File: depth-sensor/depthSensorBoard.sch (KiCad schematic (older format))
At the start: 16 parts, among them P1 CONN_02X05, P3 CONN_01X04, P4 CONN_01X04, P5 CONN_01X04, P6 CONN_01X04, Q2 Q_NJFET_GSD, U1 AP2112, U2 TCA9545A

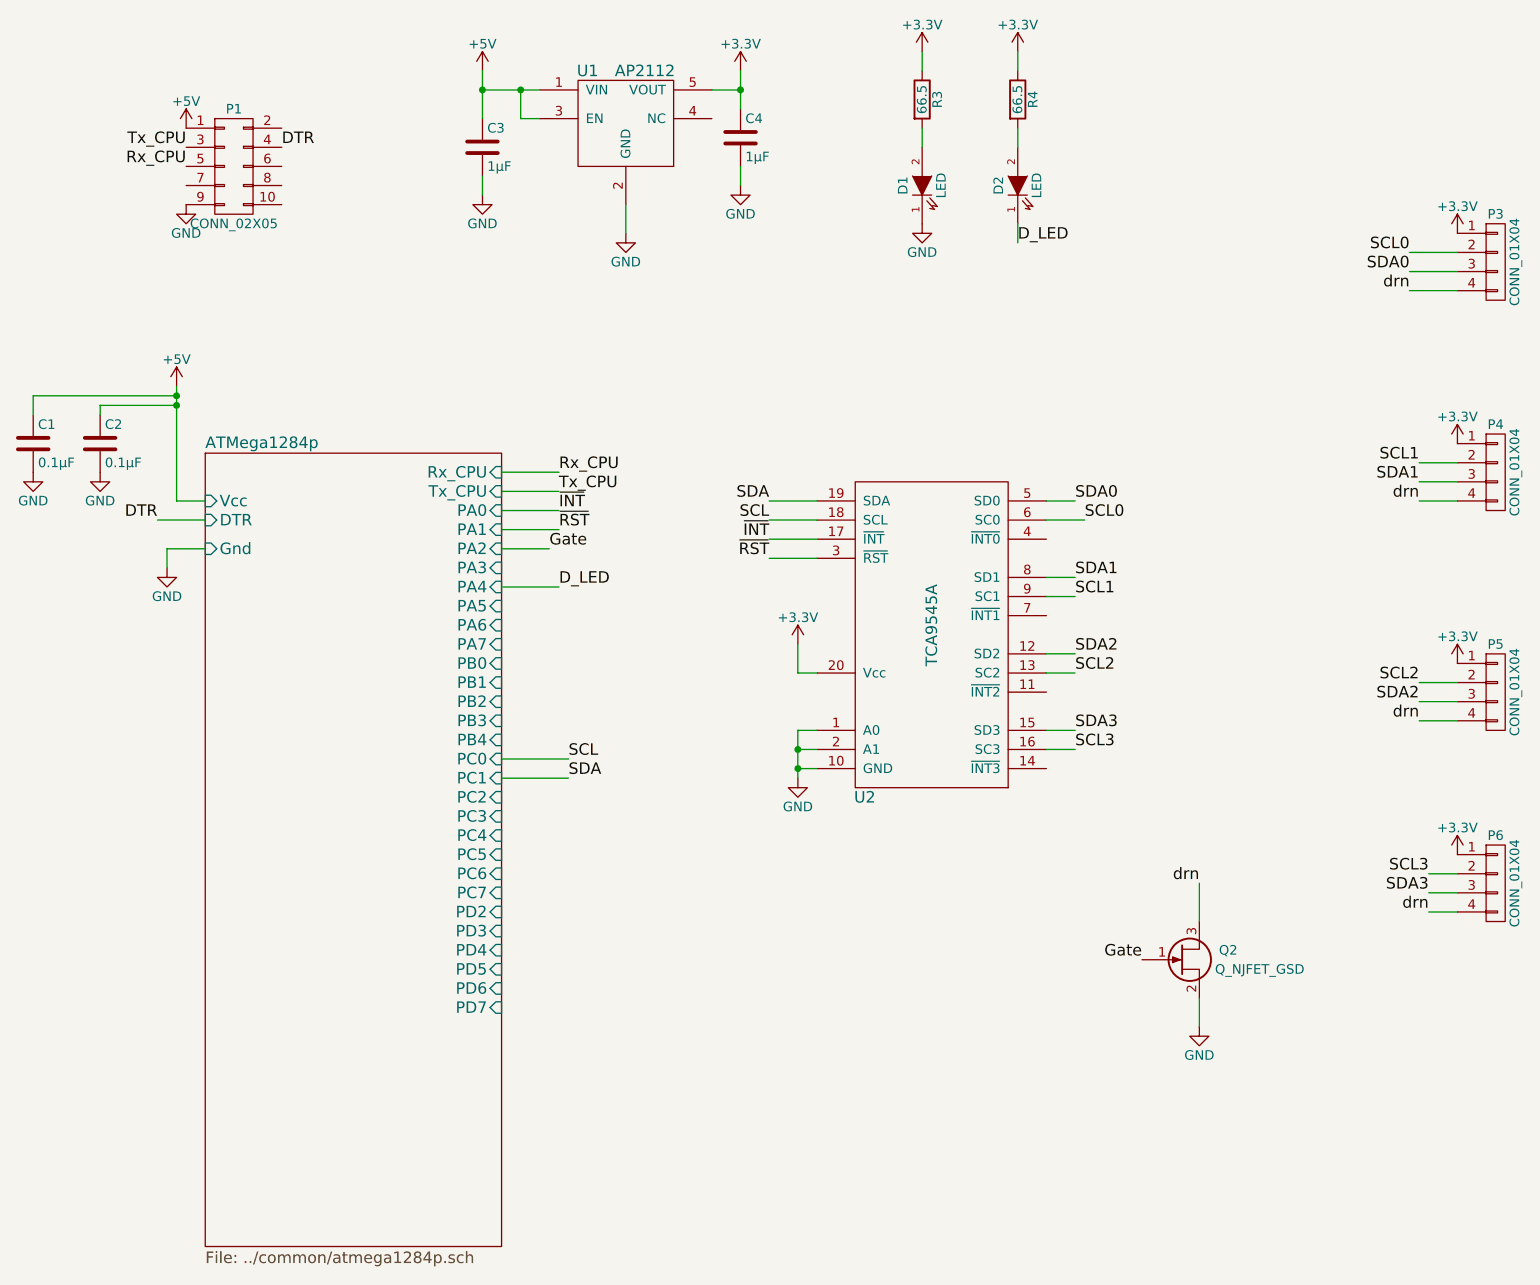
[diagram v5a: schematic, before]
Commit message: Rearranged PCB, removed LEDs from depth sensor schematic
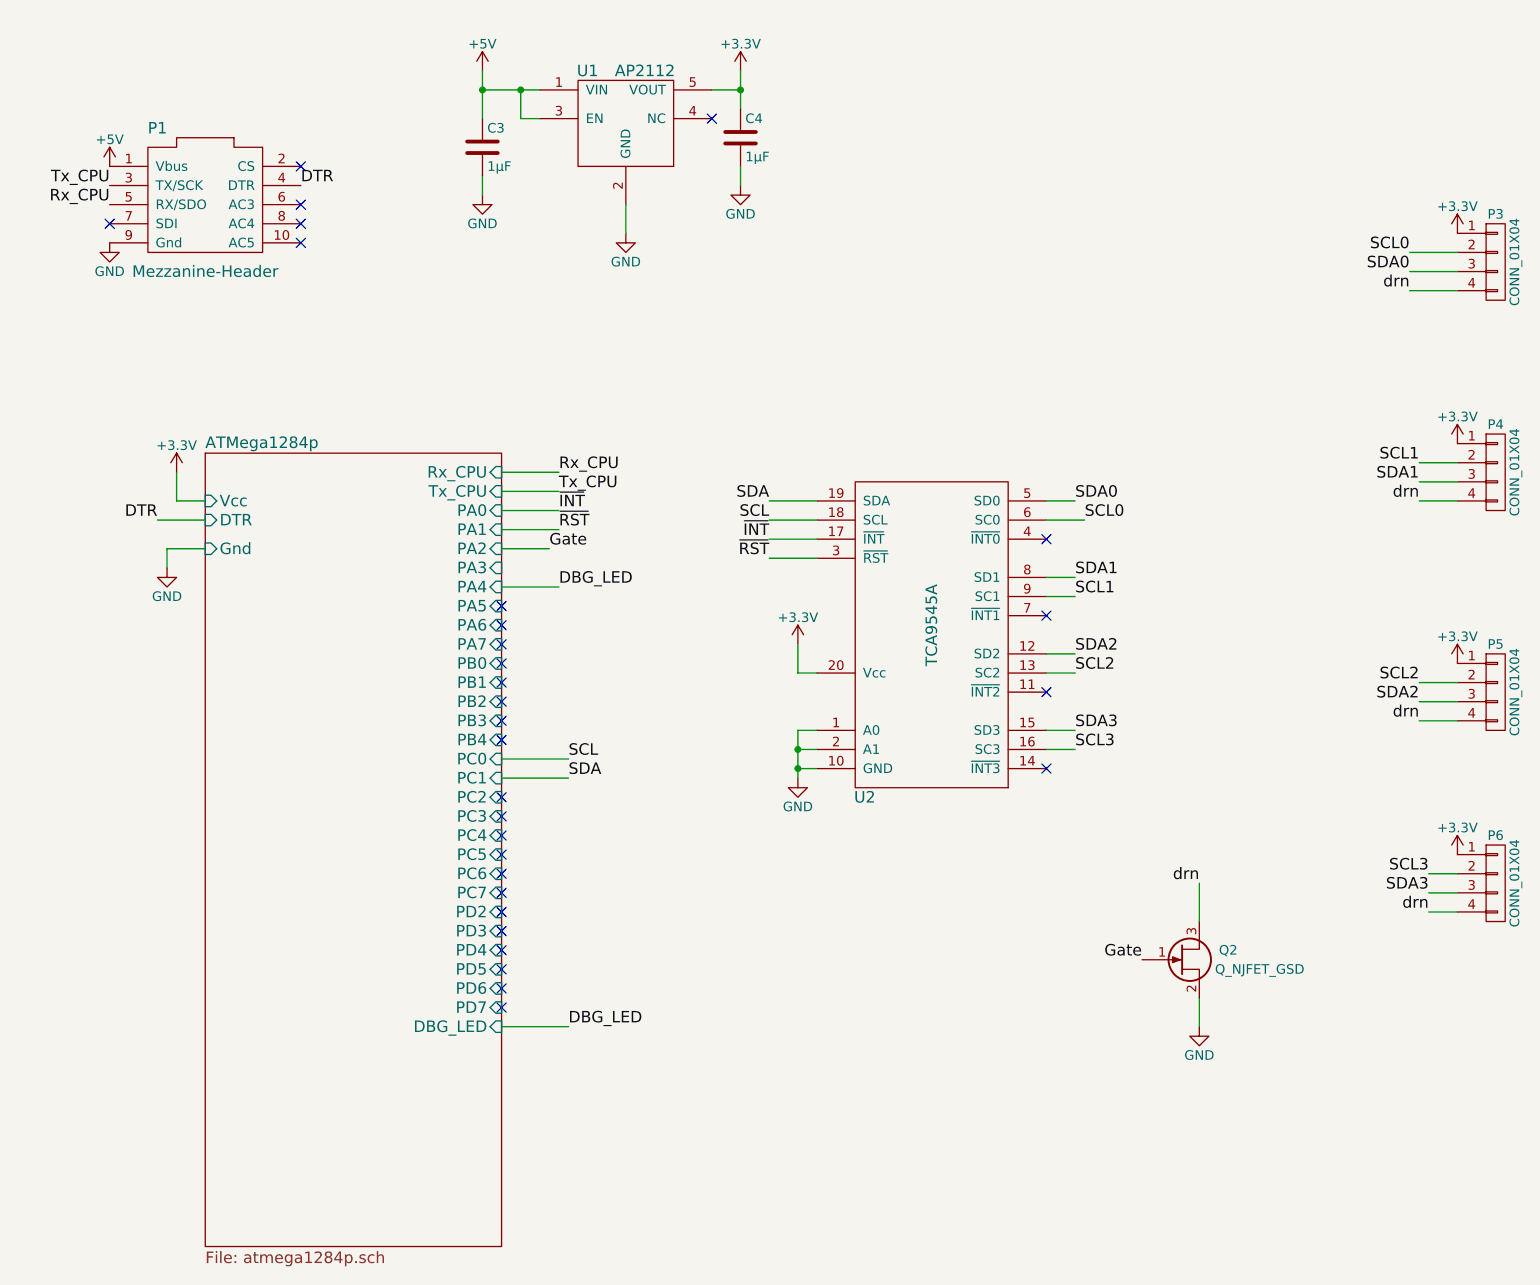
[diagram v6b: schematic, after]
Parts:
- removed C1, C2: 0.1μF, Capacitors_SMD:C_0603, symbol C
- removed D1, D2: LED, LEDs:LED_0603, symbol LED
- removed P1: CONN_02X05, robosub_footprints:DF40C-10DP-Header, symbol CONN_02X05
- removed R3, R4: 66.5, Resistors_SMD:R_0603, symbol R
- added P1: Mezzanine-Header, robosub_footprints:DF40C-10DP-Header, symbol Mezzanine-Header
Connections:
- net +5V: now also P1.1 (Vbus)
- net DTR: now also P1.4 (DTR)
- net GND: now also P1.9 (Gnd)
- net Rx_CPU: now also P1.5 (RX/SDO)
- net Tx_CPU: now also P1.3 (TX/SCK)
- no-connect marks 0 -> 30

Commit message: changed part number for mezzanine connector
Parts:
- P1: part number H11616CT-ND -> H11736TR-ND
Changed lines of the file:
@@
 F 2 "robosub_footprints:DF40C-10DP-Header" H 1150 2350 60  0001 C CNN
 F 3 "" H 1500 1950 60  0001 C CNN
-F 4 "H11616CT-ND" H 1350 2550 60  0001 C CNN "part number"
+F 4 "H11736TR-ND" H 1350 2550 60  0001 C CNN "part number"
 	1    1500 1950
 	1    0    0    -1

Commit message: Added footprint of mezzanine header/fixed routing
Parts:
- P1: footprint robosub_footprints:DF40C-10DP-Header -> robosub_footprints:3mm-10pos-receptacle
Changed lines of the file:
@@
 SCL3
 $Comp
-L GND #PWR11
+L GND #PWR01
 U 1 1 57E8E35F
 P 4600 4800
-F 0 "#PWR11" H 4600 4550 50  0001 C CNN
+F 0 "#PWR01" H 4600 4550 50  0001 C CNN
 F 1 "GND" H 4600 4650 50  0000 C CNN
 F 2 "" H 4600 4800 50  0000 C CNN
@@
 $EndComp
 $Comp
-L +3.3V #PWR10
+L +3.3V #PWR02
 U 1 1 57EC819B
 P 4600 4100
-F 0 "#PWR10" H 4600 3950 50  0001 C CNN
+F 0 "#PWR02" H 4600 3950 50  0001 C CNN
 F 1 "+3.3V" H 4600 4240 50  0000 C CNN
 F 2 "" H 4600 4100 50  0000 C CNN
@@
 SCL0
 $Comp
-L GND #PWR15
+L GND #PWR03
 U 1 1 57EE7883
 P 6700 6100
-F 0 "#PWR15" H 6700 5850 50  0001 C CNN
+F 0 "#PWR03" H 6700 5850 50  0001 C CNN
 F 1 "GND" H 6700 5950 50  0000 C CNN
 F 2 "" H 6700 6100 50  0000 C CNN
@@
 $EndComp
 $Comp
-L +3.3V #PWR16
+L +3.3V #PWR04
 U 1 1 57EE7C6C
 P 8050 1950
-F 0 "#PWR16" H 8050 1800 50  0001 C CNN
+F 0 "#PWR04" H 8050 1800 50  0001 C CNN
 F 1 "+3.3V" H 8050 2090 50  0000 C CNN
 F 2 "" H 8050 1950 50  0000 C CNN
@@
 $EndComp
 $Comp
-L +3.3V #PWR17
+L +3.3V #PWR05
 U 1 1 57EE7CA0
 P 8050 3050
-F 0 "#PWR17" H 8050 2900 50  0001 C CNN
+F 0 "#PWR05" H 8050 2900 50  0001 C CNN
 F 1 "+3.3V" H 8050 3190 50  0000 C CNN
 F 2 "" H 8050 3050 50  0000 C CNN
@@
 $EndComp
 $Comp
-L +3.3V #PWR18
+L +3.3V #PWR06
 U 1 1 57EE7DD4
 P 8050 4200
-F 0 "#PWR18" H 8050 4050 50  0001 C CNN
+F 0 "#PWR06" H 8050 4050 50  0001 C CNN
 F 1 "+3.3V" H 8050 4340 50  0000 C CNN
 F 2 "" H 8050 4200 50  0000 C CNN
@@
 $EndComp
 $Comp
-L +3.3V #PWR19
+L +3.3V #PWR07
 U 1 1 57EE7E08
 P 8050 5200
-F 0 "#PWR19" H 8050 5050 50  0001 C CNN
+F 0 "#PWR07" H 8050 5050 50  0001 C CNN
 F 1 "+3.3V" H 8050 5340 50  0000 C CNN
 F 2 "" H 8050 5200 50  0000 C CNN
@@
 $EndComp
 $Comp
-L GND #PWR3
+L GND #PWR08
 U 1 1 581C6BD6
 P 1300 3700
-F 0 "#PWR3" H 1300 3450 50  0001 C CNN
+F 0 "#PWR08" H 1300 3450 50  0001 C CNN
 F 1 "GND" H 1300 3550 50  0000 C CNN
 F 2 "" H 1300 3700 50  0000 C CNN
@@
 $EndComp
 $Comp
-L +5V #PWR5
+L +5V #PWR09
 U 1 1 58254C2A
 P 2950 1100
-F 0 "#PWR5" H 2950 950 50  0001 C CNN
+F 0 "#PWR09" H 2950 950 50  0001 C CNN
 F 1 "+5V" H 2950 1240 50  0000 C CNN
 F 2 "" H 2950 1100 50  0000 C CNN
@@
 $EndComp
 $Comp
-L +3.3V #PWR8
+L +3.3V #PWR010
 U 1 1 58257735
 P 4300 1100
-F 0 "#PWR8" H 4300 950 50  0001 C CNN
+F 0 "#PWR010" H 4300 950 50  0001 C CNN
 F 1 "+3.3V" H 4300 1240 50  0000 C CNN
 F 2 "" H 4300 1100 50  0000 C CNN
@@
 $EndComp
 $Comp
-L GND #PWR6
+L GND #PWR011
 U 1 1 5826A6AD
 P 2950 1750
-F 0 "#PWR6" H 2950 1500 50  0001 C CNN
+F 0 "#PWR011" H 2950 1500 50  0001 C CNN
 F 1 "GND" H 2950 1600 50  0000 C CNN
 F 2 "" H 2950 1750 50  0000 C CNN
@@
 $EndComp
 $Comp
-L GND #PWR9
+L GND #PWR012
 U 1 1 5826AB64
 P 4300 1700
-F 0 "#PWR9" H 4300 1450 50  0001 C CNN
+F 0 "#PWR012" H 4300 1450 50  0001 C CNN
 F 1 "GND" H 4300 1550 50  0000 C CNN
 F 2 "" H 4300 1700 50  0000 C CNN
@@
 $EndComp
 $Comp
-L GND #PWR7
+L GND #PWR013
 U 1 1 5826B4FA
 P 3700 1950
-F 0 "#PWR7" H 3700 1700 50  0001 C CNN
+F 0 "#PWR013" H 3700 1700 50  0001 C CNN
 F 1 "GND" H 3700 1800 50  0000 C CNN
 F 2 "" H 3700 1950 50  0000 C CNN
@@
 F 0 "P1" H 1250 2500 60  0000 C CNN
 F 1 "Mezzanine-Header" H 1500 1750 60  0000 C CNN
-F 2 "robosub_footprints:DF40C-10DP-Header" H 1150 2350 60  0001 C CNN
+F 2 "robosub_footprints:3mm-10pos-receptacle" H 1150 2350 60  0001 C CNN
 F 3 "" H 1500 1950 60  0001 C CNN
 F 4 "H11736TR-ND" H 1350 2550 60  0001 C CNN "part number"
@@
 $EndComp
 $Comp
-L +5V #PWR1
+L +5V #PWR014
 U 1 1 582EC117
 P 1000 1600
-F 0 "#PWR1" H 1000 1450 50  0001 C CNN
+F 0 "#PWR014" H 1000 1450 50  0001 C CNN
 F 1 "+5V" H 1000 1740 50  0000 C CNN
 F 2 "" H 1000 1600 50  0000 C CNN
@@
 DTR
 $Comp
-L GND #PWR2
+L GND #PWR015
 U 1 1 582EEC94
 P 1000 2000
-F 0 "#PWR2" H 1000 1750 50  0001 C CNN
+F 0 "#PWR015" H 1000 1750 50  0001 C CNN
 F 1 "GND" H 1000 1850 50  0000 C CNN
 F 2 "" H 1000 2000 50  0000 C CNN
@@
 	3400 6100 3050 6100
 $Comp
-L +3.3V #PWR?
+L +3.3V #PWR016
 U 1 1 582F4191
 P 1350 3200
-F 0 "#PWR?" H 1350 3050 50  0001 C CNN
+F 0 "#PWR016" H 1350 3050 50  0001 C CNN
 F 1 "+3.3V" H 1350 3340 50  0000 C CNN
 F 2 "" H 1350 3200 50  0000 C CNN
